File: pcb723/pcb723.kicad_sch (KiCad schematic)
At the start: 42 parts, among them J1 Conn_01x02_Pin, J2 Conn_01x02_Pin, J3 Conn_02x07_Odd_Even, J4 Conn_02x04_Odd_Even, SW1 SW_Push, U1 STM32H723ZGT6, U2 AMS1117-3.3, Y1 8MHz 20pF

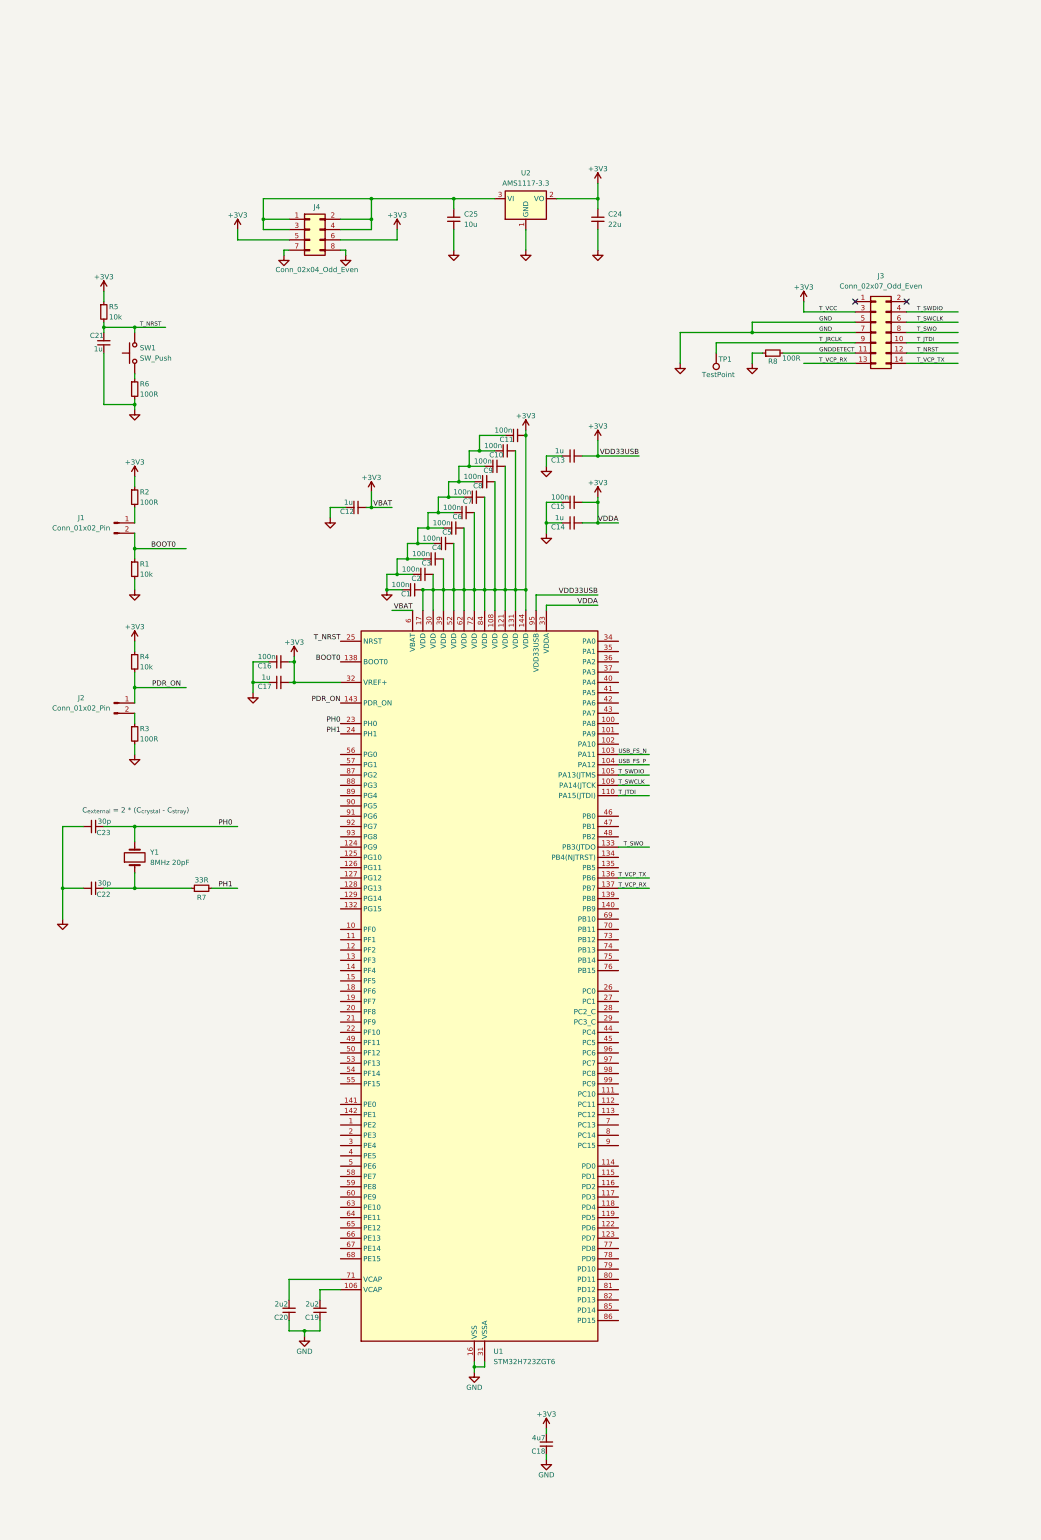
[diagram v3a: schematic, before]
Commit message: Add USB-C connector
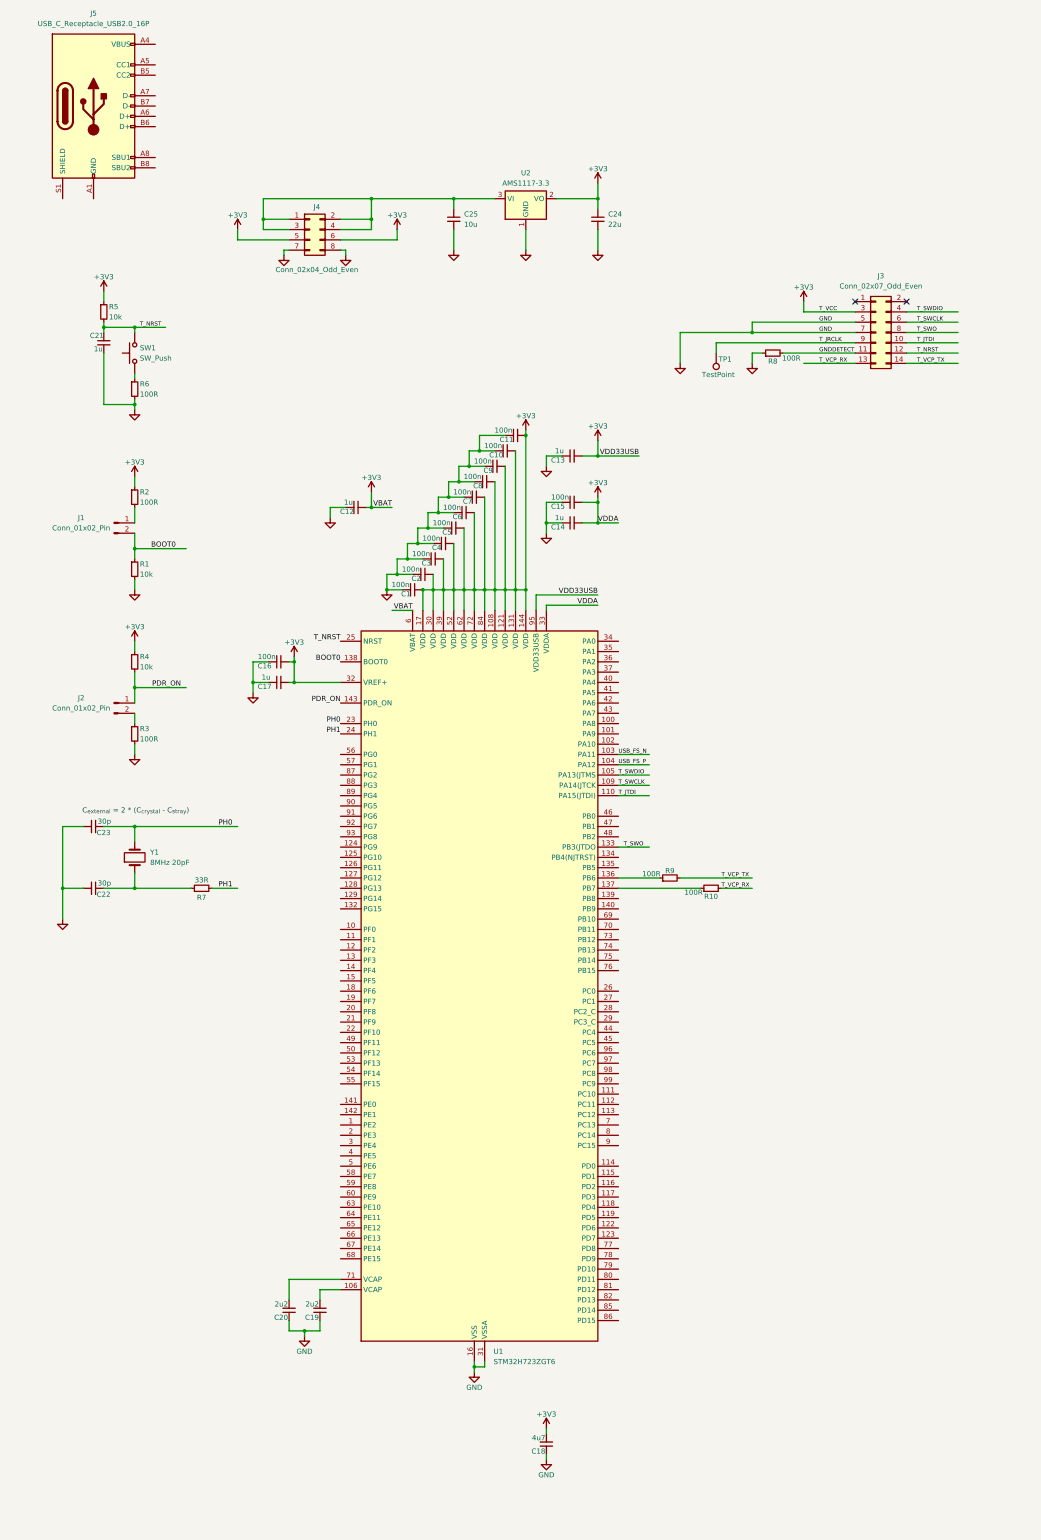
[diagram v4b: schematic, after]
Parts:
- added J5: USB_C_Receptacle_USB2.0_16P, Connector_USB:USB_C_Receptacle_GCT_USB4105-xx-A_16P_TopMnt_Horizontal, symbol Connector:USB_C_Receptacle_USB2.0_16P
- added R10, R9: 100R, Capacitor_SMD:C_0402_1005Metric, symbol Device:R_Small
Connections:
- net T_VCP_RX: now also R10.2; no longer U1.137 (PB7)
- net T_VCP_TX: now also R9.2; no longer U1.136 (PB6)
- new net: R9.1, U1.136 (PB6)
- new net: R10.1, U1.137 (PB7)
- new net: J5.A1 (GND), J5.A12 (GND), J5.B1 (GND), J5.B12 (GND)
- new net: J5.A4 (VBUS), J5.A9 (VBUS), J5.B4 (VBUS), J5.B9 (VBUS)

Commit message: Add shielding
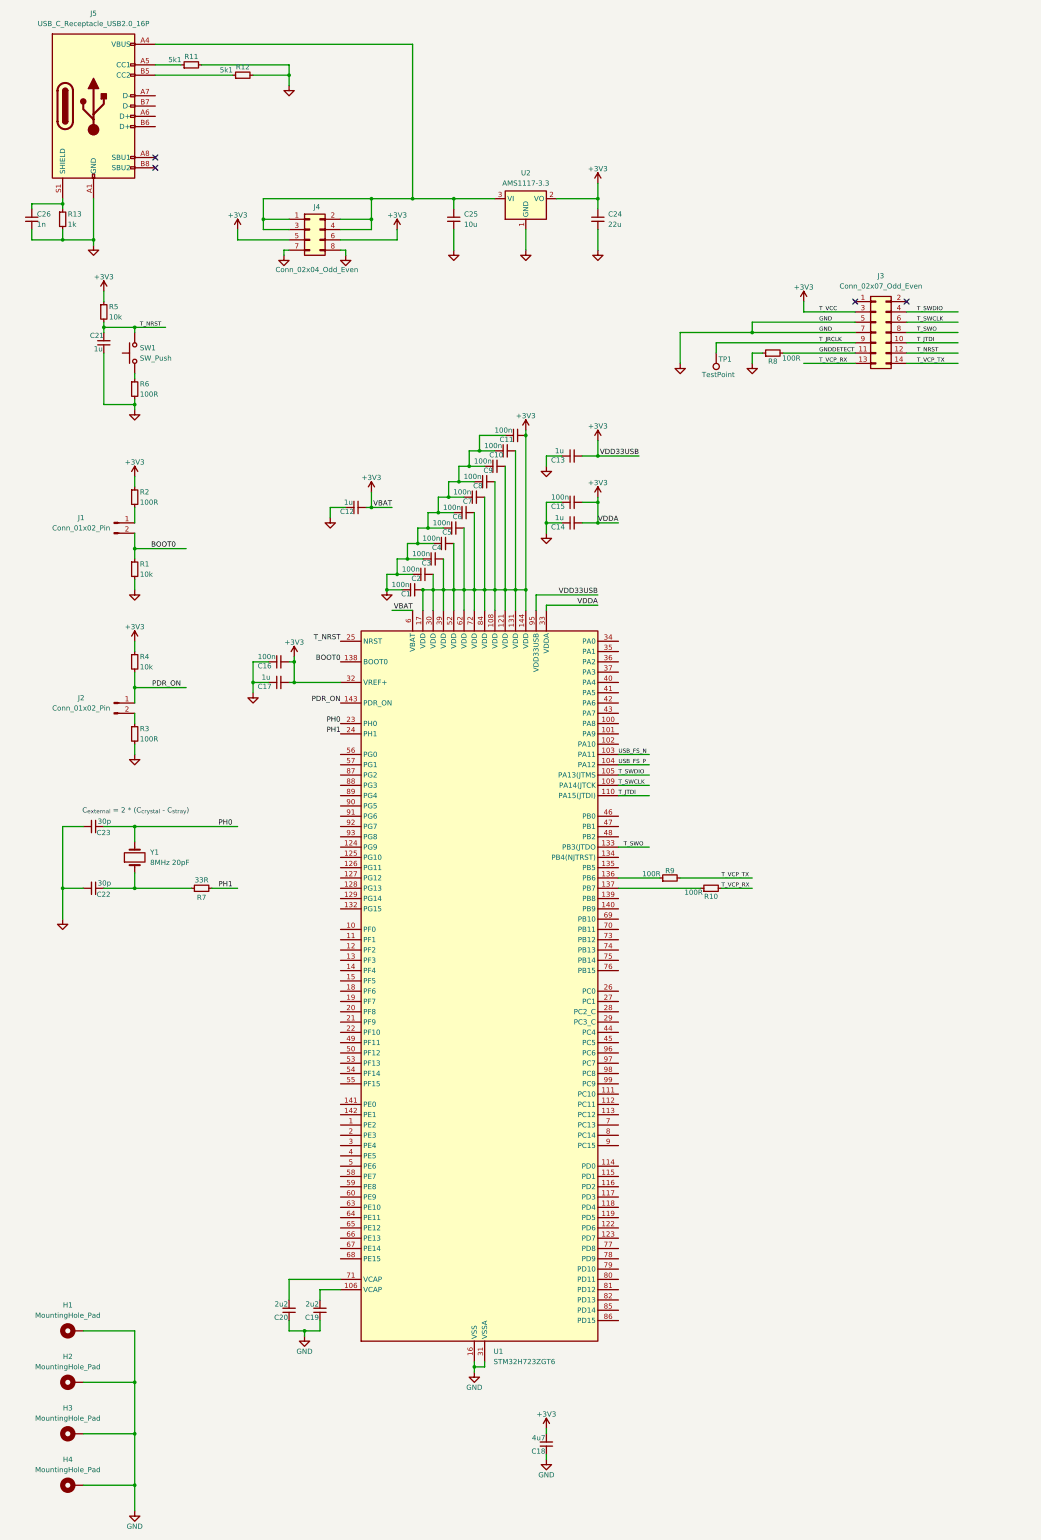
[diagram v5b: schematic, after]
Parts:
- added C26: 1n, symbol Device:C_Small
- added H1, H2, H3, H4: MountingHole_Pad, MountingHole:MountingHole_3.2mm_M3_Pad_Via, symbol Mechanical:MountingHole_Pad
- added R11, R12: 5k1, symbol Device:R_Small
- added R13: 1k, symbol Device:R_Small
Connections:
- net GND: now also J5.A1 (GND), J5.A12 (GND), J5.B1 (GND), J5.B12 (GND), C26.2, H1.1, H2.1, H3.1, H4.1, R11.2, R12.2, R13.2
- net at C25.1, J4.1 (Pin_1), J4.2 (Pin_2)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: now also J5.A4 (VBUS), J5.A9 (VBUS), J5.B4 (VBUS), J5.B9 (VBUS)
- net at J5.A5 (CC1): now also R11.1
- net at J5.B5 (CC2): now also R12.1
- net at J5.S1 (SHIELD): now also C26.1, R13.1
- no-connect marks 2 -> 4

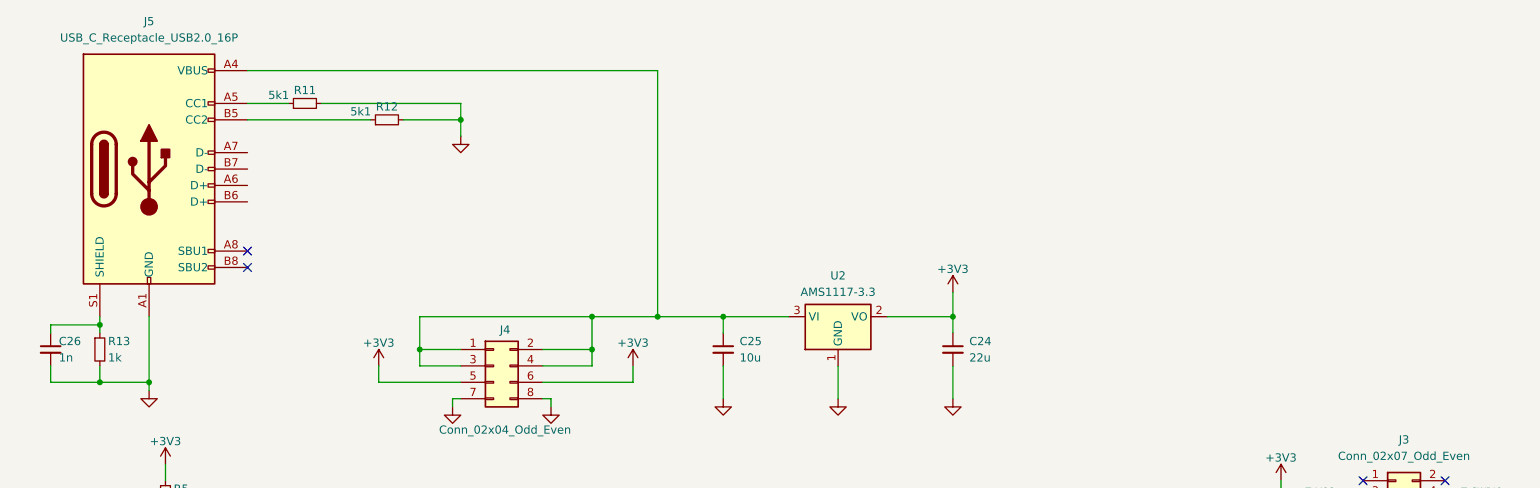
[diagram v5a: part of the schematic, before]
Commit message: Add PWR LED
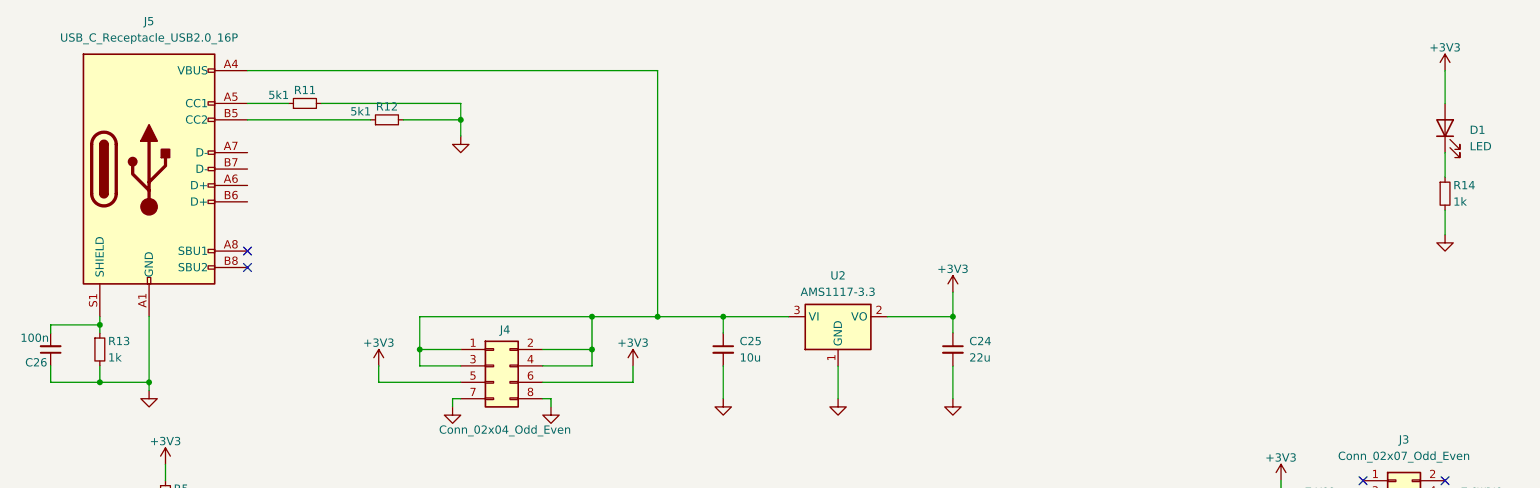
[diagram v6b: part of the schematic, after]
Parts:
- added D1: LED, LED_SMD:LED_0603_1608Metric, symbol Device:LED
- added R14: 1k, Resistor_SMD:R_0402_1005Metric, symbol Device:R_Small
- C26: value 1n -> 100n; footprint (none) -> Capacitor_SMD:C_0402_1005Metric; JLC# (none) -> C307331
- R11, R12: footprint (none) -> Resistor_SMD:R_0402_1005Metric; JLC# (none) -> C25905
- R13: footprint (none) -> Resistor_SMD:R_0402_1005Metric; JLC# (none) -> C11702
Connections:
- net +3V3: now also D1.2 (A)
- net GND: now also C26.1, R14.2; no longer C26.2
- net at J5.S1 (SHIELD), R13.1: now also C26.2; no longer C26.1
- new net: D1.1 (K), R14.1

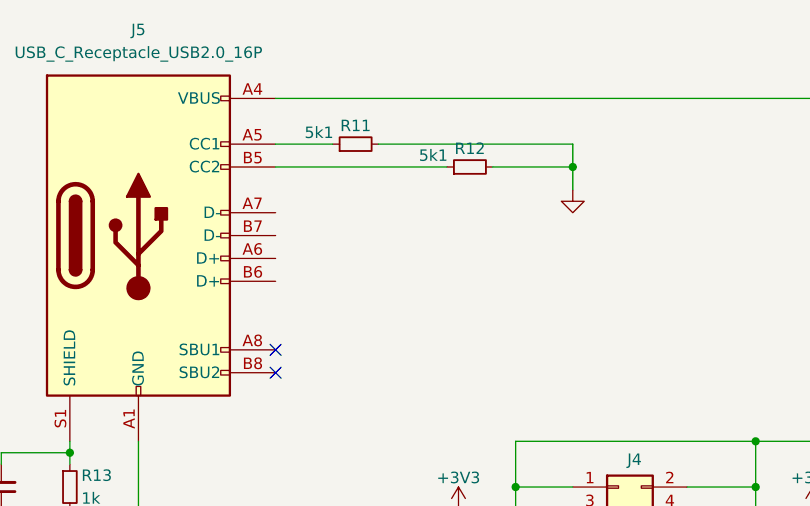
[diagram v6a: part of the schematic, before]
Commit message: Place decoupling capacitors
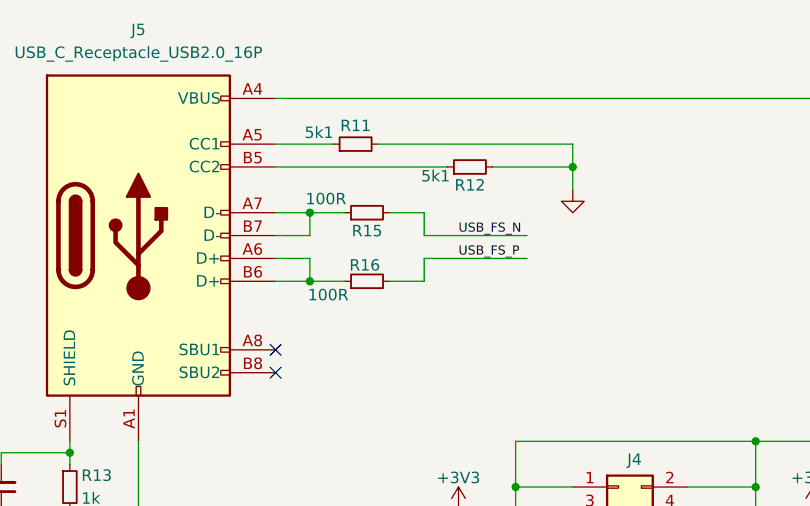
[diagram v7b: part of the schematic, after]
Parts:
- added R15, R16: 100R, Capacitor_SMD:C_0402_1005Metric, symbol Device:R_Small
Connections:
- net USB_FS_N: now also R15.2
- net USB_FS_P: now also R16.2
- net at J5.A6 (D+): now also J5.B6 (D+), R16.1
- net at J5.A7 (D-): now also J5.B7 (D-), R15.1
